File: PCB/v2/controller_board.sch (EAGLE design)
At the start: 69 parts, among them M1 B4B-PH-K-S(LF)(SN), M1_TMC TMC2209_SILENTSTEPSTICK, M2 B4B-PH-K-S(LF)(SN), M2_TMC TMC2209_SILENTSTEPSTICK, M3 B4B-PH-K-S(LF)(SN), M3_TMC TMC2209_SILENTSTEPSTICK, M4 B4B-PH-K-S(LF)(SN), M4_TMC TMC2209_SILENTSTEPSTICK

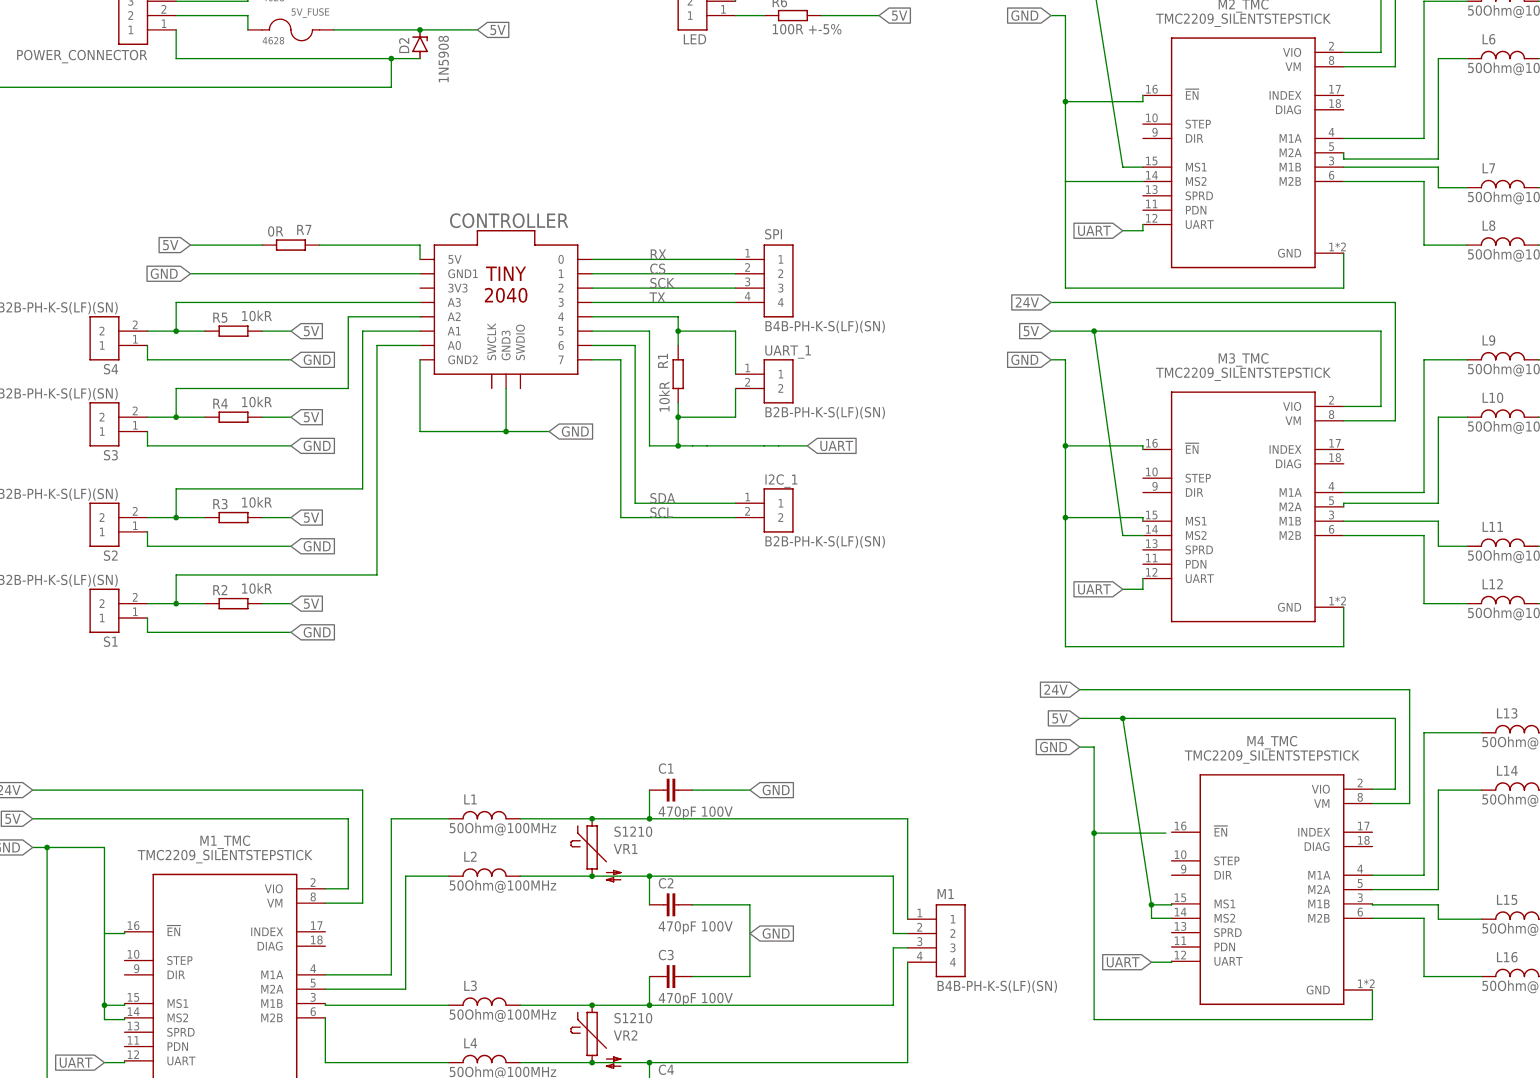
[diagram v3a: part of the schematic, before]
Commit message: feat(pcb): add wires
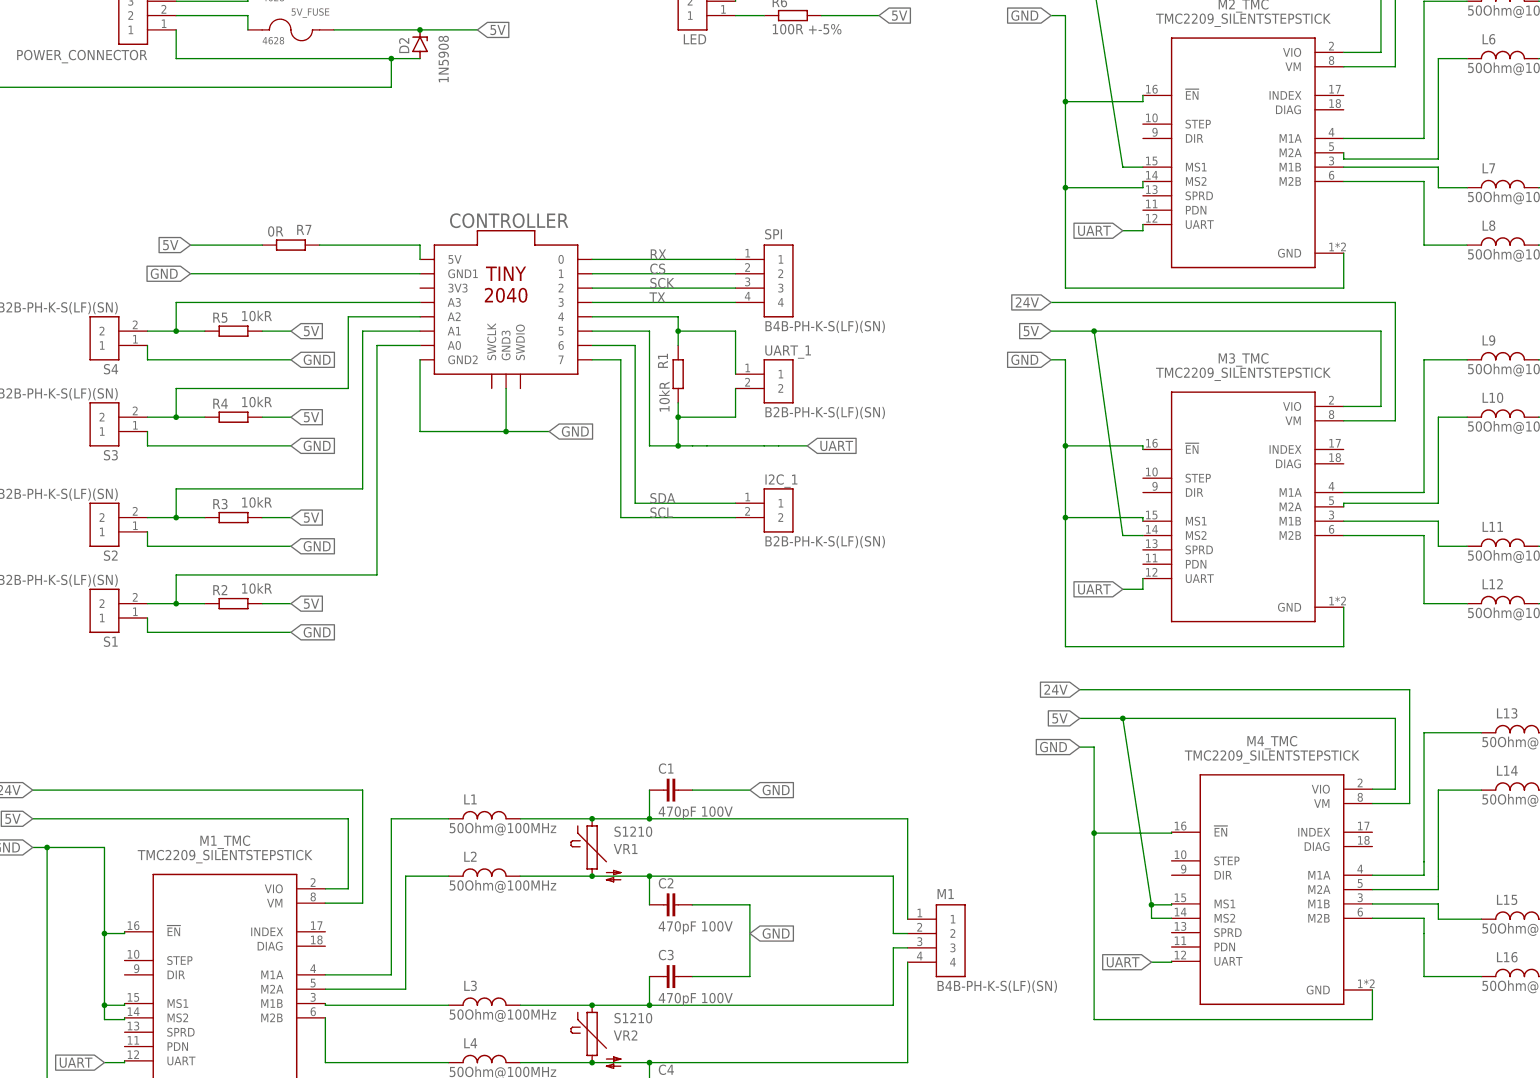
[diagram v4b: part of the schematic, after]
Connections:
- net GND: now also M4_TMC.!EN
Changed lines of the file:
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@@
 <wire x1="31.5" y1="61.26" x2="31.5" y2="60.96" width="0.1524" layer="91"/>
 <wire x1="31.5" y1="60.96" x2="27.94" y2="60.96" width="0.1524" layer="91"/>
-<pinref part="M1_TMC" gate="G$1" pin="!EN"/>
-<wire x1="31.5" y1="73.96" x2="31.5" y2="73.66" width="0.1524" layer="91"/>
-<wire x1="31.5" y1="73.66" x2="27.94" y2="73.66" width="0.1524" layer="91"/>
 <junction x="27.94" y="60.96"/>
-<wire x1="27.94" y1="73.66" x2="27.94" y2="60.96" width="0.1524" layer="91"/>
 <wire x1="27.94" y1="60.96" x2="27.94" y2="58.42" width="0.1524" layer="91"/>
 <wire x1="17.78" y1="88.9" x2="27.94" y2="88.9" width="0.1524" layer="91"/>
@@
 <junction x="17.78" y="88.9"/>
 <label x="15.24" y="88.9" size="1.778" layer="95" rot="R180" xref="yes"/>
-</segment>
-<segment>
-<pinref part="M2_TMC" gate="G$1" pin="MS2"/>
-<wire x1="211.84" y1="206.84" x2="198.12" y2="206.84" width="0.1524" layer="91"/>
-<wire x1="198.12" y1="206.84" x2="198.12" y2="220.98" width="0.1524" layer="91"/>
+<pinref part="M1_TMC" gate="G$1" pin="!EN"/>
+<wire x1="27.94" y1="73.66" x2="27.94" y2="60.96" width="0.1524" layer="91"/>
+<wire x1="27.94" y1="73.66" x2="31.5" y2="73.66" width="0.1524" layer="91"/>
+<wire x1="31.5" y1="73.66" x2="31.5" y2="73.96" width="0.1524" layer="91"/>
+<junction x="27.94" y="73.66"/>
+</segment>
+<segment>
 <wire x1="198.12" y1="220.98" x2="198.12" y2="236.22" width="0.1524" layer="91"/>
 <wire x1="198.12" y1="236.22" x2="195.58" y2="236.22" width="0.1524" layer="91"/>
@@
 <wire x1="247.4" y1="194.14" x2="247.4" y2="187.96" width="0.1524" layer="91"/>
 <wire x1="247.4" y1="187.96" x2="198.12" y2="187.96" width="0.1524" layer="91"/>
-<wire x1="198.12" y1="187.96" x2="198.12" y2="206.84" width="0.1524" layer="91"/>
+<wire x1="198.12" y1="187.96" x2="198.12" y2="205.74" width="0.1524" layer="91"/>
 <label x="195.58" y="236.22" size="1.778" layer="95" rot="R180" xref="yes"/>
+<wire x1="198.12" y1="205.74" x2="198.12" y2="220.98" width="0.1524" layer="91"/>
+<junction x="198.12" y="205.74"/>
+<pinref part="M2_TMC" gate="G$1" pin="MS2"/>
+<wire x1="198.12" y1="205.74" x2="211.84" y2="205.74" width="0.1524" layer="91"/>
+<wire x1="211.84" y1="205.74" x2="211.84" y2="206.84" width="0.1524" layer="91"/>
 </segment>
 <segment>
@@
 </segment>
 <segment>
-<wire x1="215.9" y1="91.44" x2="203.2" y2="91.44" width="0.1524" layer="91"/>
-<wire x1="203.2" y1="91.44" x2="203.2" y2="106.68" width="0.1524" layer="91"/>
 <wire x1="203.2" y1="106.68" x2="200.66" y2="106.68" width="0.1524" layer="91"/>
 <label x="200.66" y="106.68" size="1.778" layer="95" rot="R180" xref="yes"/>
@@
 <wire x1="252.48" y1="58.42" x2="203.2" y2="58.42" width="0.1524" layer="91"/>
 <wire x1="203.2" y1="58.42" x2="203.2" y2="91.44" width="0.1524" layer="91"/>
+<pinref part="M4_TMC" gate="G$1" pin="!EN"/>
+<wire x1="203.2" y1="91.44" x2="203.2" y2="106.68" width="0.1524" layer="91"/>
+<wire x1="216.92" y1="91.6" x2="216.92" y2="91.44" width="0.1524" layer="91"/>
+<wire x1="216.92" y1="91.44" x2="203.2" y2="91.44" width="0.1524" layer="91"/>
 <junction x="203.2" y="91.44"/>
 </segment>
@@
 </segment>
 </net>
-<net name="N$26" class="0">
-<segment>
-<pinref part="L1" gate="G$1" pin="1"/>
-<wire x1="88.9" y1="93.98" x2="78.74" y2="93.98" width="0.1524" layer="91"/>
-<pinref part="M1_TMC" gate="G$1" pin="M1A"/>
-<wire x1="67.06" y1="66.34" x2="78.74" y2="66.34" width="0.1524" layer="91"/>
-<wire x1="78.74" y1="66.34" x2="78.74" y2="93.98" width="0.1524" layer="91"/>
-</segment>
-</net>
-<net name="N$21" class="0">
-<segment>
-<pinref part="M1_TMC" gate="G$1" pin="M1B"/>
-<pinref part="L3" gate="G$1" pin="1"/>
-<wire x1="67.06" y1="61.26" x2="67.06" y2="60.96" width="0.1524" layer="91"/>
-<wire x1="67.06" y1="60.96" x2="88.9" y2="60.96" width="0.1524" layer="91"/>
-</segment>
-</net>
-<net name="N$27" class="0">
-<segment>
-<pinref part="M1_TMC" gate="G$1" pin="M2B"/>
-<pinref part="L4" gate="G$1" pin="1"/>
-<wire x1="67.06" y1="58.72" x2="67.06" y2="50.8" width="0.1524" layer="91"/>
-<wire x1="67.06" y1="50.8" x2="88.9" y2="50.8" width="0.1524" layer="91"/>
-</segment>
-</net>
-<net name="N$19" class="0">
-<segment>
-<pinref part="M1_TMC" gate="G$1" pin="M2A"/>
-<wire x1="67.06" y1="63.8" x2="81.28" y2="63.8" width="0.1524" layer="91"/>
-<wire x1="81.28" y1="63.8" x2="81.28" y2="83.82" width="0.1524" layer="91"/>
-<pinref part="L2" gate="G$1" pin="1"/>
-<wire x1="81.28" y1="83.82" x2="88.9" y2="83.82" width="0.1524" layer="91"/>
-</segment>
-</net>
 <net name="N$5" class="0">
 <segment>
@@
 <net name="N$36" class="0">
 <segment>
+<pinref part="L13" gate="G$1" pin="1"/>
+<wire x1="261.62" y1="86.36" x2="261.62" y2="109.22" width="0.1524" layer="91"/>
+<wire x1="261.62" y1="109.22" x2="271.78" y2="109.22" width="0.1524" layer="91"/>
 <pinref part="M4_TMC" gate="G$1" pin="M1A"/>
-<wire x1="252.48" y1="83.98" x2="261.62" y2="83.98" width="0.1524" layer="91"/>
-<wire x1="261.62" y1="83.98" x2="261.62" y2="109.22" width="0.1524" layer="91"/>
-<pinref part="L13" gate="G$1" pin="1"/>
-<wire x1="261.62" y1="109.22" x2="271.78" y2="109.22" width="0.1524" layer="91"/>
+<wire x1="261.62" y1="86.36" x2="261.62" y2="83.98" width="0.1524" layer="91"/>
+<wire x1="261.62" y1="83.98" x2="252.48" y2="83.98" width="0.1524" layer="91"/>
 </segment>
 </net>
 <net name="N$37" class="0">
 <segment>
+<pinref part="L14" gate="G$1" pin="1"/>
+<wire x1="264.16" y1="83.82" x2="264.16" y2="99.06" width="0.1524" layer="91"/>
+<wire x1="264.16" y1="99.06" x2="271.78" y2="99.06" width="0.1524" layer="91"/>
 <pinref part="M4_TMC" gate="G$1" pin="M2A"/>
-<wire x1="252.48" y1="81.44" x2="264.16" y2="81.44" width="0.1524" layer="91"/>
-<wire x1="264.16" y1="81.44" x2="264.16" y2="99.06" width="0.1524" layer="91"/>
-<pinref part="L14" gate="G$1" pin="1"/>
-<wire x1="264.16" y1="99.06" x2="271.78" y2="99.06" width="0.1524" layer="91"/>
+<wire x1="264.16" y1="83.82" x2="264.16" y2="81.44" width="0.1524" layer="91"/>
+<wire x1="264.16" y1="81.44" x2="252.48" y2="81.44" width="0.1524" layer="91"/>
 </segment>
 </net>
 <net name="N$38" class="0">
 <segment>
+<pinref part="L16" gate="G$1" pin="1"/>
+<wire x1="261.62" y1="73.66" x2="261.62" y2="66.04" width="0.1524" layer="91"/>
+<wire x1="261.62" y1="66.04" x2="271.78" y2="66.04" width="0.1524" layer="91"/>
 <pinref part="M4_TMC" gate="G$1" pin="M2B"/>
-<wire x1="252.48" y1="76.36" x2="261.62" y2="76.36" width="0.1524" layer="91"/>
-<wire x1="261.62" y1="76.36" x2="261.62" y2="66.04" width="0.1524" layer="91"/>
-<pinref part="L16" gate="G$1" pin="1"/>
-<wire x1="261.62" y1="66.04" x2="271.78" y2="66.04" width="0.1524" layer="91"/>
+<wire x1="261.62" y1="73.66" x2="261.62" y2="76.36" width="0.1524" layer="91"/>
+<wire x1="261.62" y1="76.36" x2="252.48" y2="76.36" width="0.1524" layer="91"/>
 </segment>
 </net>
 <net name="N$39" class="0">
 <segment>
-<pinref part="M4_TMC" gate="G$1" pin="M1B"/>
-<wire x1="252.48" y1="78.9" x2="252.48" y2="78.74" width="0.1524" layer="91"/>
-<wire x1="252.48" y1="78.74" x2="264.16" y2="78.74" width="0.1524" layer="91"/>
-<wire x1="264.16" y1="78.74" x2="264.16" y2="76.2" width="0.1524" layer="91"/>
+<wire x1="264.16" y1="78.9" x2="264.16" y2="76.2" width="0.1524" layer="91"/>
 <pinref part="L15" gate="G$1" pin="1"/>
 <wire x1="264.16" y1="76.2" x2="271.78" y2="76.2" width="0.1524" layer="91"/>
+<pinref part="M4_TMC" gate="G$1" pin="M1B"/>
+<wire x1="264.16" y1="78.9" x2="252.48" y2="78.9" width="0.1524" layer="91"/>
+</segment>
+</net>
+<net name="N$19" class="0">
+<segment>
+<pinref part="M1_TMC" gate="G$1" pin="M2A"/>
+<wire x1="67.06" y1="63.8" x2="81.28" y2="63.8" width="0.1524" layer="91"/>
+<wire x1="81.28" y1="63.8" x2="81.28" y2="83.82" width="0.1524" layer="91"/>
+<pinref part="L2" gate="G$1" pin="1"/>
+<wire x1="81.28" y1="83.82" x2="88.9" y2="83.82" width="0.1524" layer="91"/>
+</segment>
+</net>
+<net name="N$22" class="0">
+<segment>
+<pinref part="M1_TMC" gate="G$1" pin="M1A"/>
+<wire x1="67.06" y1="66.34" x2="78.74" y2="66.34" width="0.1524" layer="91"/>
+<wire x1="78.74" y1="66.34" x2="78.74" y2="93.98" width="0.1524" layer="91"/>
+<pinref part="L1" gate="G$1" pin="1"/>
+<wire x1="78.74" y1="93.98" x2="88.9" y2="93.98" width="0.1524" layer="91"/>
+</segment>
+</net>
+<net name="N$21" class="0">
+<segment>
+<pinref part="M1_TMC" gate="G$1" pin="M1B"/>
+<pinref part="L3" gate="G$1" pin="1"/>
+<wire x1="67.06" y1="61.26" x2="67.06" y2="60.96" width="0.1524" layer="91"/>
+<wire x1="67.06" y1="60.96" x2="88.9" y2="60.96" width="0.1524" layer="91"/>
+</segment>
+</net>
+<net name="N$26" class="0">
+<segment>
+<pinref part="M1_TMC" gate="G$1" pin="M2B"/>
+<pinref part="L4" gate="G$1" pin="1"/>
+<wire x1="67.06" y1="58.72" x2="67.06" y2="50.8" width="0.1524" layer="91"/>
+<wire x1="67.06" y1="50.8" x2="88.9" y2="50.8" width="0.1524" layer="91"/>
 </segment>
 </net>
@@
 </sheet>
 </sheets>
+<errors>
+</errors>
 </schematic>
 </drawing>

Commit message: feat(pcb): add 3V3 circuit
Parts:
- removed L1, L10, L11, L12, L13, L14, L15, L16, L2, L3, L4, L5, L6, L7, L8, L9: 50Ohm@100MHz, ngspice-simulation:L
- removed VR1, VR2, VR3, VR4, VR5, VR6, VR7, VR8: S1210, varistor:S1210
- added 3V3_FUSE1: 4628, 4628:4628
- added D3: PTVS24VS1UR, PTVS24VS1UR:PTVS24VS1UR
- added R10, R8, R9: 0R, rcl:R-EU_R0805
- added V1, V2, V3, V4, V5, V6, V7, V8: S2220, varistor:S2220
- D1: value 26V -> PTVS3V3S1UR; device diode:ZENER-DIODESMB -> PTVS3V3S1UR:PTVS3V3S1UR
- D2: value 1N5908 -> PTVS5V0S1UR; device diode:ZENER-DIODESMB -> PTVS5V0S1UR:PTVS5V0S1UR
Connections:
- removed net 5V: 5V_FUSE.2, D2.C, M1_TMC.VIO, M2_TMC.MS1, M2_TMC.VIO, M3_TMC.MS2, M3_TMC.VIO, M4_TMC.MS1, M4_TMC.MS2, M4_TMC.VIO, R2.2, R3.2, R4.2, R5.2, R6.2, R7.2
- removed net N$28: L5.1, M2_TMC.M1A
- removed net N$29: L6.1, M2_TMC.M2A
- removed net N$30: L8.1, M2_TMC.M2B
- removed net N$31: L7.1, M2_TMC.M1B
- removed net N$32: C13.2, L13.2, M4.1, VR7.1
- removed net N$33: C14.2, L14.2, M4.2, VR7.2
- removed net N$34: C15.2, L15.2, M4.3, VR8.1
- removed net N$35: C16.2, L16.2, M4.4, VR8.2
- removed net N$36: L13.1, M4_TMC.M1A
- removed net N$37: L14.1, M4_TMC.M2A
- removed net N$38: L16.1, M4_TMC.M2B
- removed net N$39: L15.1, M4_TMC.M1B
- removed net N$9: C9.2, L9.2, M3.1, VR5.1
- new net LOW_POWER: 3V3_FUSE1.2, 5V_FUSE.2, D1.C, D2.C, M1_TMC.VIO, M2_TMC.MS1, M2_TMC.VIO, M3_TMC.MS2, M3_TMC.VIO, M4_TMC.MS1, M4_TMC.MS2, M4_TMC.VIO, R10.2, R2.2, R3.2, R4.2, R5.2, R6.2, R7.2
- net 24V: now also D3.C; no longer D1.C
- net GND: now also D3.A; no longer CONTROLLER.GND3
- net N$1: now also POWER_CONNECTOR.2, R8.2, R9.2; no longer C1.2, L1.2, M1.1, VR1.1
- net N$10: now also C12.2, M3.4, M3_TMC.M2B, V6.1; no longer C10.2, L10.2, M3.2, VR5.2
- net N$11: now also M3_TMC.M1B, V6.2; no longer L11.2, VR6.1
- net N$12: now also C9.2, M3.1, M3_TMC.M1A, V5.2; no longer C12.2, L12.2, M3.4, VR6.2
- net N$13: now also C14.2, M4.2, M4_TMC.M2A, V7.1; no longer L9.1, M3_TMC.M1A
- net N$14: now also C10.2, M3.2, V5.1; no longer L10.1
- net N$15: now also C16.2, M4.4, M4_TMC.M2B, V8.1; no longer L12.1, M3_TMC.M2B
- net N$16: now also C15.2, M4.3, M4_TMC.M1B, V8.2; no longer L11.1, M3_TMC.M1B
- net N$19: now also C3.2, M1.3, M1_TMC.M1B, V2.2; no longer L2.1, M1_TMC.M2A
- net N$2: now also M1_TMC.M2A, V1.1; no longer L2.2, VR1.2
- net N$21: now also 3V3_FUSE1.1, R8.1; no longer L3.1, M1_TMC.M1B
- net N$22: now also C13.2, M4.1, M4_TMC.M1A, V7.2; no longer L1.1, M1_TMC.M1A
- net N$23: now also CONTROLLER.3V3, R10.1; no longer 5V_FUSE.1, POWER_CONNECTOR.2
- net N$26: now also C1.2, M1.1, M1_TMC.M1A, V1.2; no longer L4.1, M1_TMC.M2B
- net N$3: now also 5V_FUSE.1, R9.1; no longer C3.2, L3.2, M1.3, VR2.1
- net N$4: now also M1_TMC.M2B, V2.1; no longer L4.2, VR2.2
- net N$5: now also C6.2, M2.2, M2_TMC.M2A, V3.1; no longer C5.2, L5.2, M2.1, VR3.1
- net N$6: now also C8.2, M2.4, M2_TMC.M2B, V4.1; no longer C6.2, L6.2, M2.2, VR3.2
- net N$7: now also M2_TMC.M1B, V4.2; no longer L7.2, VR4.1
- net N$8: now also C5.2, M2.1, M2_TMC.M1A, V3.2; no longer C8.2, L8.2, M2.4, VR4.2
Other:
- moved on the sheet: 24V_FUSE, 5V_FUSE, C1, C10, C11, C12, C13, C14, C15, C16, C2, C3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
